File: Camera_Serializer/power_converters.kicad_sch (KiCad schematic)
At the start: 9 parts, among them U3 TPS62133RGTR

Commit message: Finished power converters
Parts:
- added C23: 22uF, Capacitor_SMD:C_0603_1608Metric_Pad1.08x0.95mm_HandSolder, symbol Device:C_Small
- added C24: 10uF, Capacitor_SMD:C_0805_2012Metric_Pad1.18x1.45mm_HandSolder, symbol Device:C_Small
- added C25: 0.1uF, Capacitor_SMD:C_0402_1005Metric_Pad0.74x0.62mm_HandSolder, symbol Device:C_Small
- added C26: 3.3nF, Capacitor_SMD:C_0402_1005Metric_Pad0.74x0.62mm_HandSolder, symbol Device:C_Small
- added C27, C28, C29, C30: 1uF, symbol Device:C_Small
- added L5: 2.2uH, CameraServer_Footprints:IFSC1515AHER2R2M01, symbol Device:L
- added R19: 100k, Resistor_SMD:R_0402_1005Metric_Pad0.72x0.64mm_HandSolder, symbol Device:R_Small
- added TP7, TP8: TestPoint, TestPoint:TestPoint_Pad_D2.0mm, symbol Connector:TestPoint
- added U4: TPS62131RGTT, Snapeda:RGT0016C, symbol Snapeda:TPS62131RGTT
- added U5: ~, CameraServer_Footprints:NCP114ASN120T1G, symbol CameraServer_Symbols:NCP114ASN120T1G
- added U6: MIC5528-3.3YMT-TR, Snapeda:TDFN6_1P2X1P2_MCH, symbol Snapeda:MIC5528-3.3YMT-TR
- C22: footprint (none) -> Capacitor_SMD:C_0603_1608Metric_Pad1.08x0.95mm_HandSolder
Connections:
- net +12V: now also C24.1, C25.1, U4.10 (AVIN), U4.11 (PVIN), U4.12 (PVIN), U4.13 (EN)
- net +5V: now also C27.1, C30.1, U5.1 (IN), U5.3 (EN), U6.4 (EN), U6.6 (VIN)
- net GND: now also C23.2, C24.2, C25.2, C26.1, C27.2, C28.2, C29.2, C30.2, TP8.1, U4.15 (PGND), U4.16 (PGND), U4.17 (EP), U4.5 (FB), U4.6 (AGND), U4.7 (FSW), U4.8 (DEF), U5.2 (GND), U6.3 (GND), U6.7 (EPAD)
- new net: L5.1, U4.1 (SW), U4.2 (SW), U4.3 (SW)
- new net: R19.2, TP7.1, U4.4 (PG)
- new net: C26.2, U4.9 (SS_TR)
- new net +1V2: C28.1, U5.5 (OUT)
- new net +1V8: C23.1, L5.2, R19.1, U4.14 (VOS)
- new net +3V3: C29.1, U6.1 (VOUT), U6.2 (VOUT)
- no-connect marks 0 -> 1
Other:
- note added: "1.8V Buck"
- note added: "5V Buck"
- note added: "5V to 1.2V LDO"
- note added: "5V to 3.3V LDO"
- moved on the sheet: C19, C20, C21, C22, L4, R18, TP5, TP6, U3

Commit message: Finishe schematic
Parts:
- added D2, D3, D4: GREEN, LED_SMD:LED_0603_1608Metric_Pad1.05x0.95mm_HandSolder, symbol Device:LED
- added Q1, Q2: BSS138, Package_TO_SOT_SMD:SOT-23, symbol Transistor_FET:BSS138
- added R20: 330, Resistor_SMD:R_0603_1608Metric_Pad0.98x0.95mm_HandSolder, symbol Device:R
- added R21, R24: 820, Resistor_SMD:R_0603_1608Metric_Pad0.98x0.95mm_HandSolder, symbol Device:R
- added R22, R23: 100k, Resistor_SMD:R_0402_1005Metric_Pad0.72x0.64mm_HandSolder, symbol Device:R_Small
- C27, C28, C29, C30: footprint (none) -> Capacitor_SMD:C_0402_1005Metric_Pad0.74x0.62mm_HandSolder
- TP5, TP6, TP7, TP8: footprint TestPoint:TestPoint_Pad_D2.0mm -> TestPoint:TestPoint_Pad_D1.0mm
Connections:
- net +1V2: now also Q1.1 (G), R22.1
- net +1V8: now also Q2.1 (G), R23.1
- net +3V3: now also D2.2 (A)
- net +5V: now also D3.2 (A), D4.2 (A)
- net GND: now also Q1.2 (S), Q2.2 (S), R20.2, R22.2, R23.2
- new net: D2.1 (K), R20.1
- new net: D4.1 (K), R24.1
- new net: Q2.3 (D), R24.2
- new net: D3.1 (K), R21.1
- new net: Q1.3 (D), R21.2
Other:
- moved on the sheet: C23, C24, C25, C26, C29, C30, L5, R19, TP7, TP8, U4, U6

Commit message: Layout started
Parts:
- U4: footprint Snapeda:RGT0016C -> CameraServer_Footprints:TPS62133RGTR
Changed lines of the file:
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@@
 			)
 		)
-		(property "Footprint" "Snapeda:RGT0016C"
+		(property "Footprint" "CameraServer_Footprints:TPS62133RGTR"
 			(at 66.04 142.24 0)
 			(effects

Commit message: Switched out 1.2V LDO for better one
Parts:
- removed U5: ~, CameraServer_Footprints:NCP114ASN120T1G, symbol CameraServer_Symbols:NCP114ASN120T1G
- added U5: TPS73601DBVR, CameraServer_Footprints:TPS73601DBVR, symbol CameraServer_Symbols:TPS73601DBVR
- C20: footprint Capacitor_SMD:C_0805_2012Metric_Pad1.18x1.45mm_HandSolder -> Capacitor_SMD:C_0805_2012Metric
- L4, L5: footprint CameraServer_Footprints:IFSC1515AHER2R2M01 -> Inductor_SMD:L_1008_2520Metric
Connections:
- net +1V2: now also U5.5 (OUT)
- net +1V8: now also C27.1, U5.1 (IN), U5.3 (EN), U5.4 (NR/FB)
- net +5V: no longer C27.1
- net GND: now also U5.2 (GND)
- no-connect marks 1 -> 0
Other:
- note added: "1.8V Buck 1A"
- note added: "1.8V to 1.2V LDO 300mA"
- note added: "5V Buck 1A"
- note added: "F = ~2.25 MHz @ 1A Voltage ripple = ~0.01V @ 1A"
- note added: "With 2.25 MHz ripple voltage and 0.01V amplitude We expect ripple rejection of ~52dB 52dB = 20log(0.01/V_ripple_out) V_ripple_out = 31.6 uV"
- note removed: "1.8V Buck"
- note removed: "5V Buck"
- note removed: "5V to 1.2V LDO"
- moved on the sheet: C27, C28

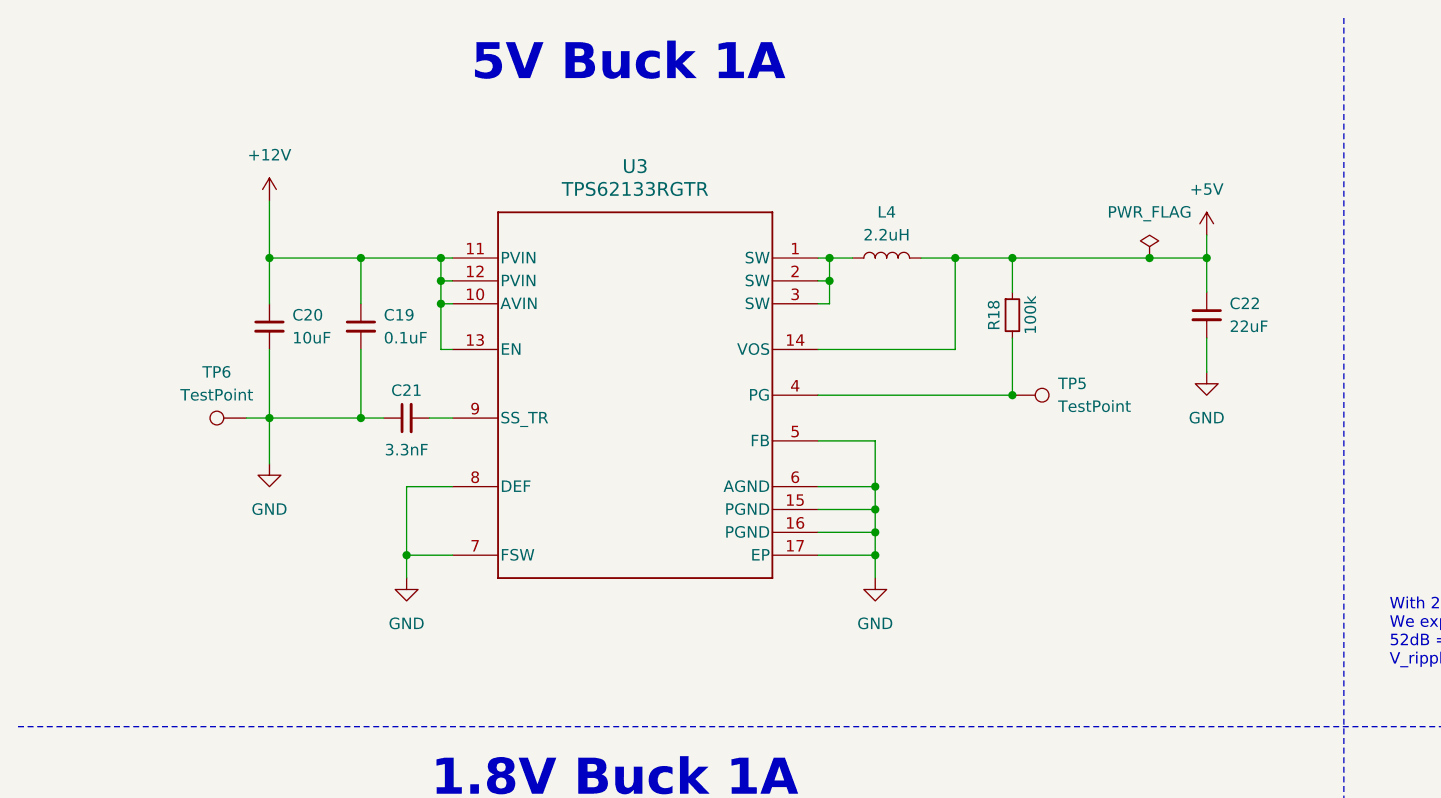
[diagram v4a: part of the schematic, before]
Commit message: All components placed in correct positions
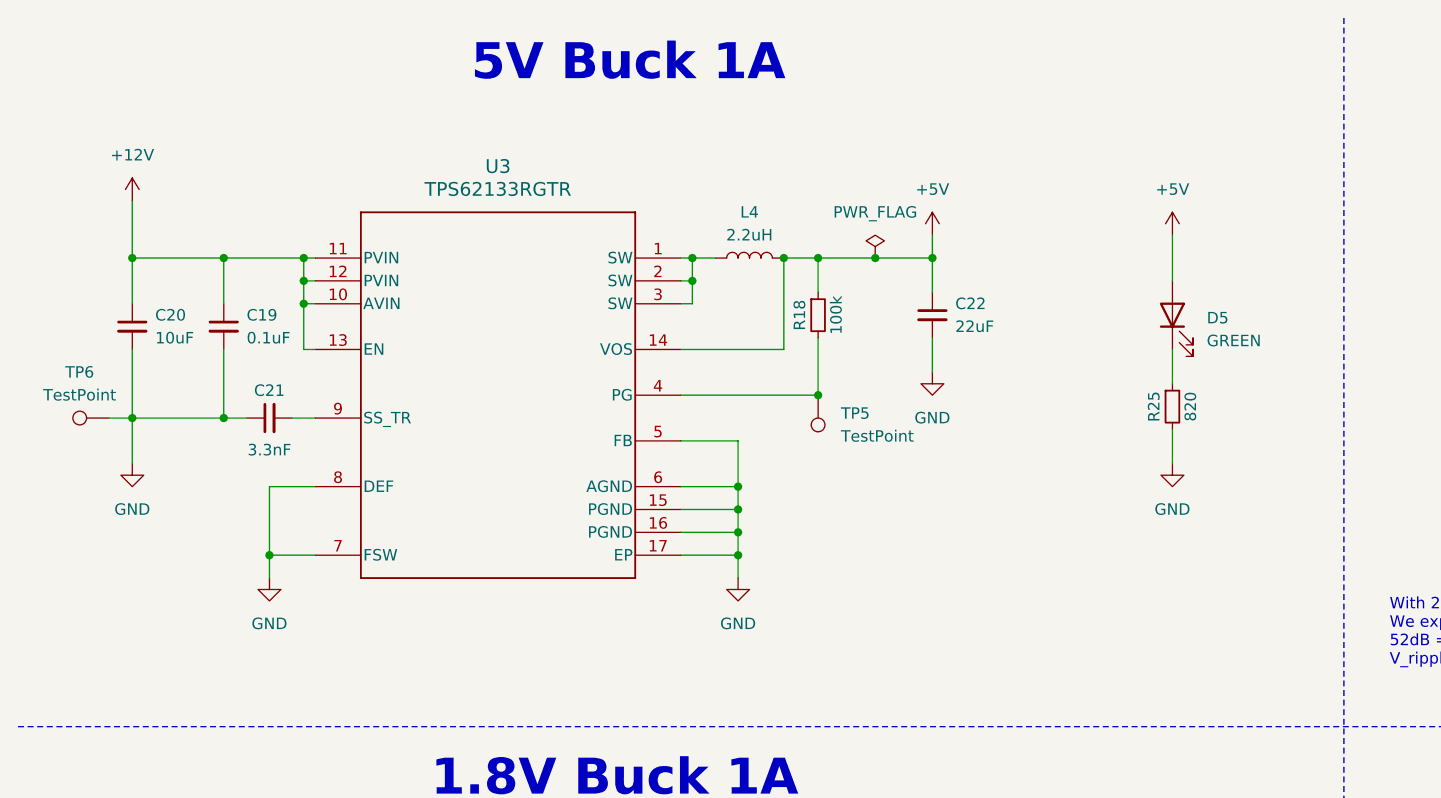
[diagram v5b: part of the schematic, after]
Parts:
- added D5: GREEN, LED_SMD:LED_0603_1608Metric_Pad1.05x0.95mm_HandSolder, symbol Device:LED
- added R25: 820, Resistor_SMD:R_0603_1608Metric_Pad0.98x0.95mm_HandSolder, symbol Device:R_Small
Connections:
- net +5V: now also D5.2 (A)
- net GND: now also R25.2
- new net: D5.1 (K), R25.1
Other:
- moved on the sheet: C19, C20, C21, C22, L4, R18, TP5, TP6, U3

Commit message: Finished routing
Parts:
- removed TP6: TestPoint, TestPoint:TestPoint_Pad_D1.0mm, symbol Connector:TestPoint
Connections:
- net GND: now also C21.2; no longer C21.1
- net at U3.9 (SS_TR): now also C21.1; no longer C21.2
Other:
- moved on the sheet: C21
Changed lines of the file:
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@@
-	(wire
-		(pts
-			(xy 25.4 57.15) (xy 22.86 57.15)
-		)
-		(stroke
-			(width 0)
-			(type default)
-		)
-	)
 	(wire
 		(pts
@@
 	)
 	(symbol
-		(lib_id "Connector:TestPoint")
-		(at 22.86 57.15 90)
-		(unit 1)
-		(exclude_from_sim no)
-		(in_bom yes)
-		(on_board yes)
-		(dnp no)
-		(fields_autoplaced yes)
-		(property "Reference" "TP6"
-			(at 19.558 52.07 90)
-			(effects
-				(font
-					(size 1.27 1.27)
-				)
-			)
-		)
-		(property "Value" "TestPoint"
-			(at 19.558 54.61 90)
-			(effects
-				(font
-					(size 1.27 1.27)
-				)
-			)
-		)
-		(property "Footprint" "TestPoint:TestPoint_Pad_D1.0mm"
-			(at 22.86 52.07 0)
-			(effects
-				(font
-					(size 1.27 1.27)
-				)
-				(hide yes)
-			)
-		)
-		(property "Datasheet" "~"
-			(at 22.86 52.07 0)
-			(effects
-				(font
-					(size 1.27 1.27)
-				)
-				(hide yes)
-			)
-		)
-		(property "Description" "test point"
-			(at 22.86 57.15 0)
-			(effects
-				(font
-					(size 1.27 1.27)
-				)
-				(hide yes)
-			)
-		)
-		(pin "1"
-		)
-		(instances
-			(project "Camera_serializer"
-				(path "/ebaf1619-da94-4b8e-b57a-a386470e666e/aa1b48ff-d467-42b0-a250-5333a1eca37c"
-					(reference "TP6")
-					(unit 1)
-				)
-			)
-		)
-	)
-	(symbol
 		(lib_id "power:+3V3")
 		(at 171.45 120.65 0)
@@
 	(symbol
 		(lib_id "Device:C_Small")
-		(at 40.64 57.15 90)
-		(unit 1)
-		(exclude_from_sim no)
+		(at 40.64 57.15 270)
+		(mirror x)
+		(unit 1)
+		(exclude_from_sim no)

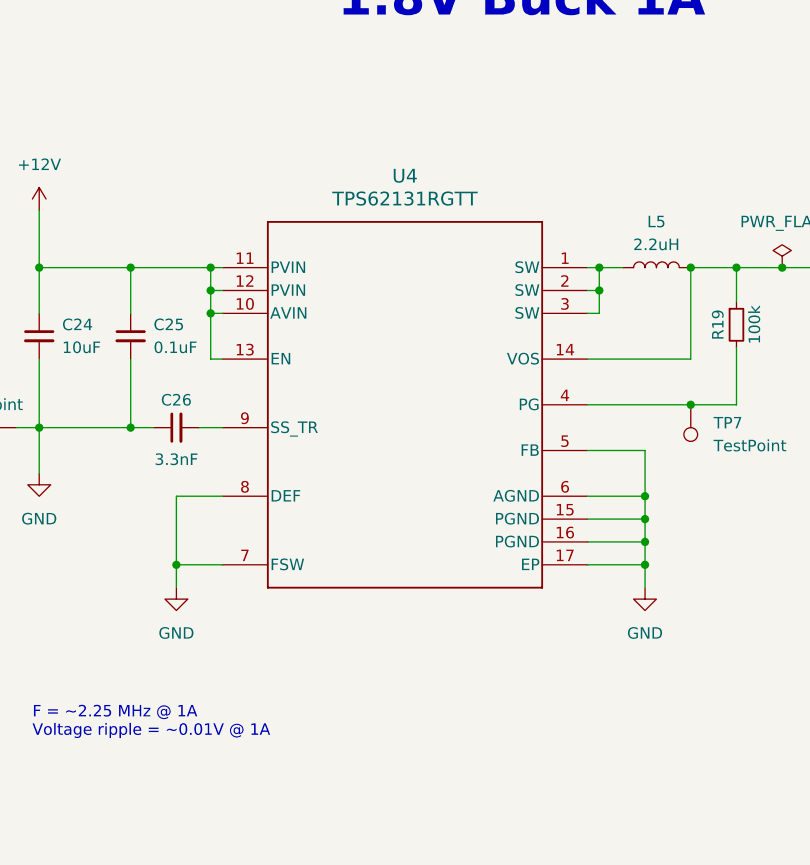
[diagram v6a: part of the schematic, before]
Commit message: Finished differential routing
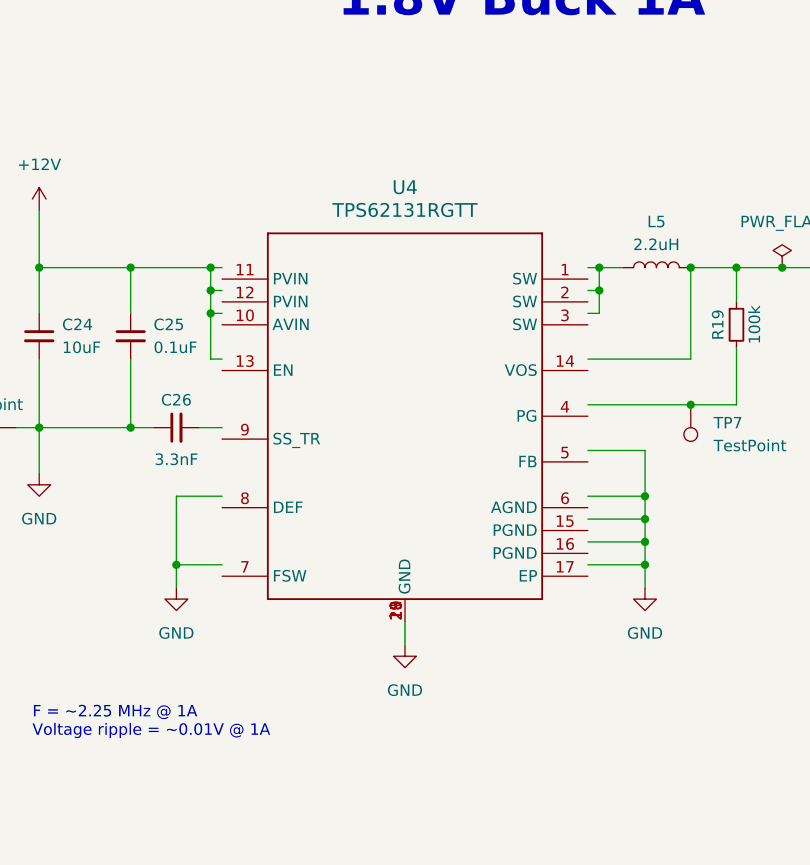
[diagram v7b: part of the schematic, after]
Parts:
- U4: symbol Snapeda:TPS62131RGTT -> CameraServer_Symbols:TPS62131RGTT
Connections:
- net +12V: no longer U4.10 (AVIN), U4.11 (PVIN), U4.12 (PVIN), U4.13 (EN)
- net +1V8: no longer U4.14 (VOS)
- net GND: now also U4.18 (GND), U4.19 (GND), U4.20 (GND), U4.21 (GND); no longer U4.15 (PGND), U4.16 (PGND), U4.17 (EP), U4.5 (FB), U4.6 (AGND), U4.7 (FSW), U4.8 (DEF)
- net at R19.2, TP7.1: no longer U4.4 (PG)
- net at U4.9 (SS_TR): no longer C26.2
- now unconnected: L5.1, U4.1 (SW), U4.2 (SW), U4.3 (SW)
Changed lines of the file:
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@@
 	(wire
 		(pts
+			(xy 66.04 166.37) (xy 66.04 168.91)
+		)
+		(stroke
+			(width 0)
+			(type default)
+		)
+	)
+	(wire
+		(pts
 			(xy 102.87 127) (xy 102.87 130.81)
 		)
@@
 	)
 	(symbol
-		(lib_id "Snapeda:TPS62131RGTT")
+		(lib_id "CameraServer_Symbols:TPS62131RGTT")
 		(at 66.04 142.24 0)
 		(unit 1)
@@
 		(fields_autoplaced yes)
 		(property "Reference" "U4"
-			(at 66.04 116.84 0)
+			(at 66.04 118.11 0)
 			(effects
 				(font
@@
 		)
 		(property "Value" "TPS62131RGTT"
-			(at 66.04 119.38 0)
+			(at 66.04 120.65 0)
 			(effects
 				(font
@@
 				(font
 					(size 1.27 1.27)
-					(italic yes)
 				)
 				(hide yes)
@@
 				(font
 					(size 1.27 1.27)
-					(italic yes)
 				)
 				(hide yes)
@@
 		(pin "14"
 		)
+		(pin "21"
+		)
+		(pin "18"
+		)
+		(pin "19"
+		)
+		(pin "20"
+		)
 		(instances
 			(project ""
@@
 					(unit 1)
 				)
+			)
+		)
+	)
+	(symbol
+		(lib_id "power:GND")
+		(at 66.04 168.91 0)
+		(unit 1)
+		(exclude_from_sim no)
+		(in_bom yes)
+		(on_board yes)
+		(dnp no)
+		(fields_autoplaced yes)
+		(property "Reference" "#PWR058"
+			(at 66.04 175.26 0)
+			(effects
+				(font
+					(size 1.27 1.27)
+				)
+				(hide yes)
+			)
+		)
+		(property "Value" "GND"
+			(at 66.04 173.99 0)
+			(effects
+				(font
+					(size 1.27 1.27)
+				)
+			)
+		)
+		(property "Footprint" ""
+			(at 66.04 168.91 0)
+			(effects
+				(font
+					(size 1.27 1.27)
+				)
+				(hide yes)
+			)
+		)
+		(property "Datasheet" ""
+			(at 66.04 168.91 0)
+			(effects
+				(font
+					(size 1.27 1.27)
+				)
+				(hide yes)
+			)
+		)
+		(property "Description" "Power symbol creates a global label with name \"GND\" , ground"
+			(at 66.04 168.91 0)
+			(effects
+				(font
+					(size 1.27 1.27)
+				)
+				(hide yes)
+			)
+		)
+		(pin "1"
+		)
+		(instances
+			(project "Camera_serializer"
+				(path "/ebaf1619-da94-4b8e-b57a-a386470e666e/aa1b48ff-d467-42b0-a250-5333a1eca37c"
+					(reference "#PWR058")
+					(unit 1)
+				)

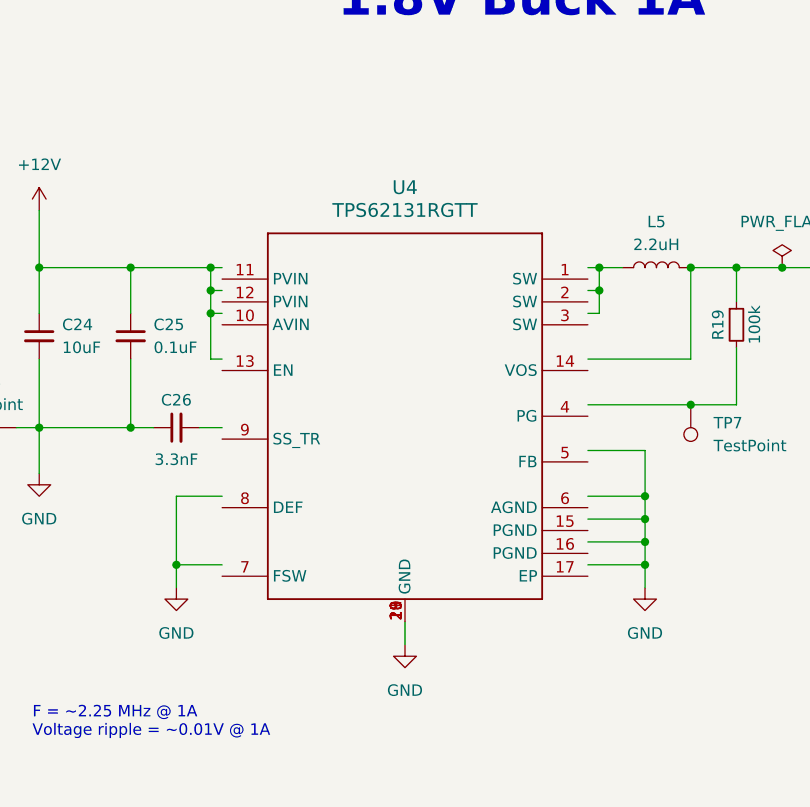
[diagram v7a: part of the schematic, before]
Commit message: Fixed power IC disconnected on schematic
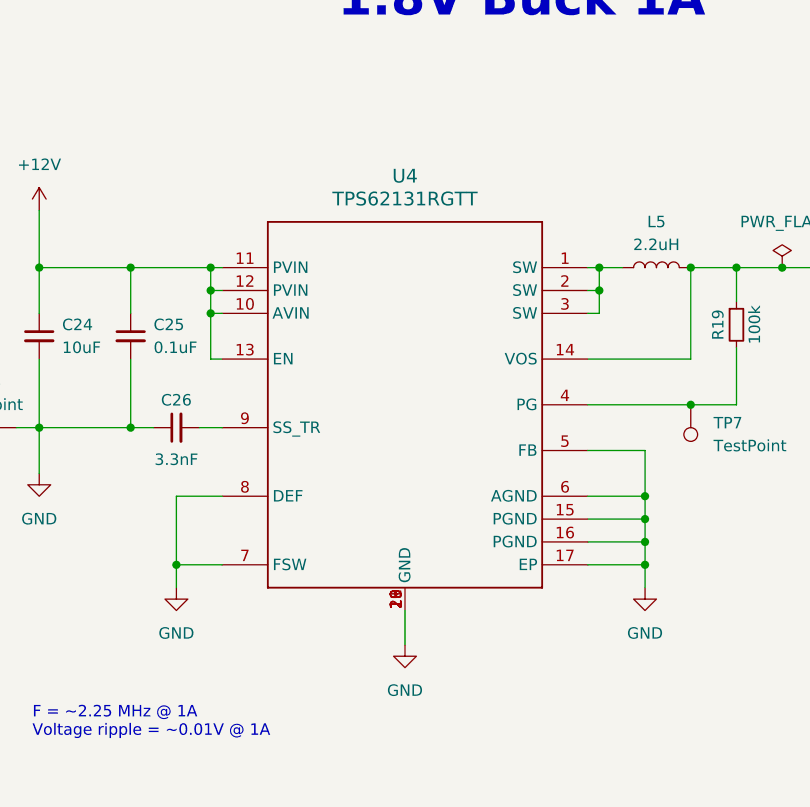
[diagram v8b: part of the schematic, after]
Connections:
- net +12V: now also U4.10 (AVIN), U4.11 (PVIN), U4.12 (PVIN), U4.13 (EN)
- net +1V8: now also U4.14 (VOS)
- net GND: now also U4.15 (PGND), U4.16 (PGND), U4.17 (EP), U4.5 (FB), U4.6 (AGND), U4.7 (FSW), U4.8 (DEF)
- net at L5.1: now also U4.1 (SW), U4.2 (SW), U4.3 (SW)
- net at U4.4 (PG): now also R19.2, TP7.1
- net at U4.9 (SS_TR): now also C26.2
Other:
- moved on the sheet: U4
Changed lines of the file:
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@@
 	(wire
 		(pts
-			(xy 66.04 166.37) (xy 66.04 168.91)
+			(xy 66.04 165.1) (xy 66.04 168.91)
 		)
 		(stroke
@@
 	(symbol
 		(lib_id "CameraServer_Symbols:TPS62131RGTT")
-		(at 66.04 142.24 0)
+		(at 66.04 140.97 0)
 		(unit 1)
 		(exclude_from_sim no)
@@
 		(fields_autoplaced yes)
 		(property "Reference" "U4"
-			(at 66.04 118.11 0)
+			(at 66.04 116.84 0)
 			(effects
 				(font
@@
 		)
 		(property "Value" "TPS62131RGTT"
-			(at 66.04 120.65 0)
+			(at 66.04 119.38 0)
 			(effects
 				(font
@@
 		)
 		(property "Footprint" "CameraServer_Footprints:TPS62133RGTR"
-			(at 66.04 142.24 0)
+			(at 66.04 140.97 0)
 			(effects
 				(font
@@
 		)
 		(property "Datasheet" "https://www.ti.com/lit/ds/symlink/tps62131.pdf?HQS=dis-dk-null-digikeymode-dsf-pf-null-wwe&ts=1735498025028"
-			(at 66.04 142.24 0)
+			(at 66.04 140.97 0)
 			(effects
 				(font
@@
 		)
 		(property "Description" ""
-			(at 66.04 142.24 0)
-			(effects
-				(font
+			(at 66.04 140.97 0)
+			(effects
+				(font
